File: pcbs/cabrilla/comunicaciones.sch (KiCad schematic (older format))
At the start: 6 parts, among them J8 UART_lora, U3 LoRa, Y2 LoRa

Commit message: Added STM32
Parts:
- added R14: 10k, Resistor_SMD:R_0805_2012Metric_Pad1.15x1.40mm_HandSolder, symbol Device:R
- added SW1: SW_Push, Button_Switch_SMD:SW_Push_1P1T_NO_6x6mm_H9.5mm, symbol Switch:SW_Push
- C6: renamed from C4; footprint Capacitor_SMD:C_0805_2012Metric -> Capacitor_SMD:C_0805_2012Metric_Pad1.15x1.40mm_HandSolder
- C7: renamed from C5; footprint Capacitor_SMD:C_0805_2012Metric -> Capacitor_SMD:C_0805_2012Metric_Pad1.15x1.40mm_HandSolder
- U3: renamed from U?; footprint (none) -> elementos:lorabee
- renumbered U3 to COM1, J8 to deb_com1
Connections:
- net +3V3: now also U3.1 (3.3v), R14.1
- net GND: now also U3.10 (GND), SW1.2
- net rx_lora: now also COM1.3 (PD1); no longer COM1.2 (PD0)
- net tx_lora: now also COM1.2 (PD0); no longer COM1.3 (PD1)
- net at COM1.1 (PC6/~RESET): now also R14.2, SW1.1
- net SS_lora: now reaches COM1.16 (PB2)
- net SS_lora: now also U3.17 (NSS)
- net MOSI: now reaches COM1.17 (PB3)
- net MOSI: now also U3.11 (MOSI)
- net MISO: now reaches COM1.18 (PB4)
- net MISO: now also U3.4 (MISO)
- net SCK: now reaches COM1.19 (PB5)
- net SCK: now also U3.18 (SCK)
- no-connect marks 0 -> 12
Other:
- note added: "rx, tx con respecto al STM32\n"
- moved on the sheet: U3
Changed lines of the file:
@@
 	4800 4250 5100 4250
 Text Label 5100 4150 2    50   ~ 0
+tx_lora
+Text Label 5100 4250 2    50   ~ 0
 rx_lora
-Text Label 5100 4250 2    50   ~ 0
-tx_lora
 Connection ~ 4250 5300
 Wire Wire Line
@@
 P 4250 5300
 AR Path="/5D8B0DC7" Ref="#PWR?"  Part="1"
-AR Path="/5D8ABBE4/5D8B0DC7" Ref="#PWR015"  Part="1"
-F 0 "#PWR015" H 4250 5050 50  0001 C CNN
+AR Path="/5D8ABBE4/5D8B0DC7" Ref="#PWR025"  Part="1"
+F 0 "#PWR025" H 4250 5050 50  0001 C CNN
 F 1 "GND" H 4255 5127 50  0000 C CNN
 F 2 "" H 4250 5300 50  0001 C CNN
@@
 $EndComp
 $Comp
-L MCU_Microchip_ATmega:ATmega8A-PU U?
+L MCU_Microchip_ATmega:ATmega8A-PU COM?
 U 1 1 5D8B0DCF
 P 4200 3850
-AR Path="/5D8B0DCF" Ref="U?"  Part="1"
-AR Path="/5D8ABBE4/5D8B0DCF" Ref="U3"  Part="1"
-F 0 "U3" H 4200 5431 50  0000 C CNN
+AR Path="/5D8B0DCF" Ref="COM?"  Part="1"
+AR Path="/5D8ABBE4/5D8B0DCF" Ref="COM1"  Part="1"
+F 0 "COM1" H 4200 5431 50  0000 C CNN
 F 1 "LoRa" H 4200 5340 50  0000 C CNN
 F 2 "Package_DIP:DIP-28_W7.62mm_Socket" H 4200 3850 50  0001 C CIN
@@
 P 1450 6400
 AR Path="/5D989311/5D8B0DDD" Ref="C?"  Part="1"
-AR Path="/5D8ABBE4/5D8B0DDD" Ref="C5"  Part="1"
-F 0 "C5" V 1290 6400 50  0000 C CNN
+AR Path="/5D8ABBE4/5D8B0DDD" Ref="C7"  Part="1"
+F 0 "C7" V 1290 6400 50  0000 C CNN
 F 1 "22pF" V 1199 6400 50  0000 C CNN
-F 2 "Capacitor_SMD:C_0805_2012Metric" H 1488 6250 50  0001 C CNN
+F 2 "Capacitor_SMD:C_0805_2012Metric_Pad1.15x1.40mm_HandSolder" H 1488 6250 50  0001 C CNN
 F 3 "~" H 1450 6400 50  0001 C CNN
 	1    1450 6400
@@
 P 1150 6400
 AR Path="/5D989311/5D8B0DE3" Ref="C?"  Part="1"
-AR Path="/5D8ABBE4/5D8B0DE3" Ref="C4"  Part="1"
-F 0 "C4" V 1402 6400 50  0000 C CNN
+AR Path="/5D8ABBE4/5D8B0DE3" Ref="C6"  Part="1"
+F 0 "C6" V 1402 6400 50  0000 C CNN
 F 1 "22pF" V 1311 6400 50  0000 C CNN
-F 2 "Capacitor_SMD:C_0805_2012Metric" V 1310 6400 50  0001 C CNN
+F 2 "Capacitor_SMD:C_0805_2012Metric_Pad1.15x1.40mm_HandSolder" V 1310 6400 50  0001 C CNN
 F 3 "~" H 1150 6400 50  0001 C CNN
 	1    1150 6400
@@
 P 1300 6650
 AR Path="/5D989311/5D8B0DF1" Ref="#PWR?"  Part="1"
-AR Path="/5D8ABBE4/5D8B0DF1" Ref="#PWR013"  Part="1"
-F 0 "#PWR013" H 1300 6400 50  0001 C CNN
+AR Path="/5D8ABBE4/5D8B0DF1" Ref="#PWR027"  Part="1"
+F 0 "#PWR027" H 1300 6400 50  0001 C CNN
 F 1 "GND" H 1305 6477 50  0000 C CNN
 F 2 "" H 1300 6650 50  0001 C CNN
@@
 $EndComp
 Text HLabel 5100 4150 2    50   Input ~ 0
+tx_lora
+Text HLabel 5100 4250 2    50   Input ~ 0
 rx_lora
-Text HLabel 5100 4250 2    50   Input ~ 0
-tx_lora
 Text Label 1450 5900 1    50   ~ 0
 osc_2
@@
 osc_1
 $Comp
-L Connector:Conn_01x03_Male J?
+L Connector:Conn_01x03_Male deb_com?
 U 1 1 5D8B0AA2
 P 2750 6200
-AR Path="/5D8B0AA2" Ref="J?"  Part="1"
-AR Path="/5D8ABBE4/5D8B0AA2" Ref="J8"  Part="1"
-F 0 "J8" V 2812 6013 50  0000 R CNN
+AR Path="/5D8B0AA2" Ref="deb_com?"  Part="1"
+AR Path="/5D8ABBE4/5D8B0AA2" Ref="deb_com1"  Part="1"
+F 0 "deb_com1" V 2812 6013 50  0000 R CNN
 F 1 "UART_lora" V 2903 6013 50  0000 R CNN
 F 2 "Connector_PinHeader_2.54mm:PinHeader_1x03_P2.54mm_Vertical" H 2750 6200 50  0001 C CNN
@@
 P 2850 6500
 AR Path="/5D8B0AAB" Ref="#PWR?"  Part="1"
-AR Path="/5D8ABBE4/5D8B0AAB" Ref="#PWR014"  Part="1"
-F 0 "#PWR014" H 2850 6250 50  0001 C CNN
+AR Path="/5D8ABBE4/5D8B0AAB" Ref="#PWR026"  Part="1"
+F 0 "#PWR026" H 2850 6250 50  0001 C CNN
 F 1 "GND" H 2855 6327 50  0000 C CNN
 F 2 "" H 2850 6500 50  0001 C CNN
@@
 $EndComp
 $Comp
-L power:+3.3V #PWR0102
+L power:+3.3V #PWR022
 U 1 1 5D8AD624
 P 4250 2150
-F 0 "#PWR0102" H 4250 2000 50  0001 C CNN
+F 0 "#PWR022" H 4250 2000 50  0001 C CNN
 F 1 "+3.3V" H 4265 2323 50  0000 C CNN
 F 2 "" H 4250 2150 50  0001 C CNN
@@
 $EndComp
 $Comp
-L elementos:lorabee U?
+L elementos:lorabee U3
 U 1 1 5D8B69A5
-P 8150 2150
-F 0 "U?" H 8150 2415 50  0000 C CNN
-F 1 "lorabee" H 8150 2324 50  0000 C CNN
-F 2 "" H 8150 1050 50  0001 C CNN
-F 3 "" H 8150 1050 50  0001 C CNN
-	1    8150 2150
-	1    0    0    -1
-$EndComp
+P 8650 2700
+F 0 "U3" H 8650 2965 50  0000 C CNN
+F 1 "lorabee" H 8650 2874 50  0000 C CNN
+F 2 "elementos:lorabee" H 8650 1600 50  0001 C CNN
+F 3 "" H 8650 1600 50  0001 C CNN
+	1    8650 2700
+	1    0    0    -1
+$EndComp
+Text Notes 5100 4100 0    50   ~ 0
+rx, tx con respecto al STM32\n
+Wire Wire Line
+	4800 2950 5150 2950
+Wire Wire Line
+	4800 3050 5150 3050
+Wire Wire Line
+	4800 3150 5150 3150
+Wire Wire Line
+	4800 3250 5150 3250
+Text Label 5150 2950 2    50   ~ 0
+SS_lora
+Text Label 5150 3050 2    50   ~ 0
+MOSI
+Text Label 5150 3150 2    50   ~ 0
+MISO
+Text Label 5150 3250 2    50   ~ 0
+SCK
+Wire Wire Line
+	9050 3000 9350 3000
+Wire Wire Line
+	9050 3600 9250 3600
+Wire Wire Line
+	8250 3000 8050 3000
+Wire Wire Line
+	9050 2900 9200 2900
+Text Label 9350 3000 2    50   ~ 0
+SS_lora
+Text Label 9250 3600 2    50   ~ 0
+MOSI
+Text Label 8050 3000 0    50   ~ 0
+MISO
+Text Label 9200 2900 2    50   ~ 0
+SCK
+$Comp
+L power:+3.3V #PWR023
+U 1 1 5D8F4B83
+P 8150 2700
+F 0 "#PWR023" H 8150 2550 50  0001 C CNN
+F 1 "+3.3V" H 8165 2873 50  0000 C CNN
+F 2 "" H 8150 2700 50  0001 C CNN
+F 3 "" H 8150 2700 50  0001 C CNN
+	1    8150 2700
+	1    0    0    -1
+$EndComp
+Wire Wire Line
+	8250 2700 8150 2700
+$Comp
+L power:GND #PWR024
+U 1 1 5D8F6C16
+P 8150 3600
+F 0 "#PWR024" H 8150 3350 50  0001 C CNN
+F 1 "GND" H 8155 3427 50  0000 C CNN
+F 2 "" H 8150 3600 50  0001 C CNN
+F 3 "" H 8150 3600 50  0001 C CNN
+	1    8150 3600
+	1    0    0    -1
+$EndComp
+Wire Wire Line
+	8250 3600 8150 3600
+NoConn ~ 8250 2800
+NoConn ~ 8250 3200
+NoConn ~ 8250 3300
+NoConn ~ 8250 3400
+NoConn ~ 8250 3500
+NoConn ~ 9050 3400
+NoConn ~ 9050 3300
+NoConn ~ 9050 3200
+NoConn ~ 9050 3100
+NoConn ~ 9050 2800
+NoConn ~ 9050 2700
+NoConn ~ 8250 2900
+$Comp
+L Switch:SW_Push SW1
+U 1 1 5D92194B
+P 2250 2950
+F 0 "SW1" V 2204 3098 50  0000 L CNN
+F 1 "SW_Push" V 2295 3098 50  0000 L CNN
+F 2 "Button_Switch_SMD:SW_Push_1P1T_NO_6x6mm_H9.5mm" H 2250 3150 50  0001 C CNN
+F 3 "~" H 2250 3150 50  0001 C CNN
+	1    2250 2950
+	0    1    1    0
+$EndComp
+$Comp
+L Device:R R14
+U 1 1 5D92303F
+P 2250 2600
+F 0 "R14" H 2320 2646 50  0000 L CNN
+F 1 "10k" H 2320 2555 50  0000 L CNN
+F 2 "Resistor_SMD:R_0805_2012Metric_Pad1.15x1.40mm_HandSolder" V 2180 2600 50  0001 C CNN
+F 3 "~" H 2250 2600 50  0001 C CNN
+	1    2250 2600
+	1    0    0    -1
+$EndComp
+Connection ~ 2250 2750
+Wire Wire Line
+	2250 2750 3600 2750
+$Comp
+L power:GND #PWR0113
+U 1 1 5D924AFA
+P 2250 3150
+F 0 "#PWR0113" H 2250 2900 50  0001 C CNN
+F 1 "GND" H 2255 2977 50  0000 C CNN
+F 2 "" H 2250 3150 50  0001 C CNN
+F 3 "" H 2250 3150 50  0001 C CNN
+	1    2250 3150
+	1    0    0    -1
+$EndComp
+$Comp
+L power:+3.3V #PWR0114
+U 1 1 5D924E3E
+P 2250 2450
+F 0 "#PWR0114" H 2250 2300 50  0001 C CNN
+F 1 "+3.3V" H 2265 2623 50  0000 C CNN
+F 2 "" H 2250 2450 50  0001 C CNN
+F 3 "" H 2250 2450 50  0001 C CNN
+	1    2250 2450
+	1    0    0    -1
+$EndComp

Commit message: ixed
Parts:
- Y2: footprint Crystal:Crystal_HC49-4H_Vertical -> Crystal:Crystal_SMD_HC49-SD
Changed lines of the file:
@@
 F 0 "Y2" H 1300 6318 50  0000 C CNN
 F 1 "LoRa" H 1300 6227 50  0000 C CNN
-F 2 "Crystal:Crystal_HC49-4H_Vertical" H 1300 6050 50  0001 C CNN
+F 2 "Crystal:Crystal_SMD_HC49-SD" H 1300 6050 50  0001 C CNN
 F 3 "~" H 1300 6050 50  0001 C CNN
 	1    1300 6050

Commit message: 80
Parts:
- Y2: footprint Crystal:Crystal_SMD_HC49-SD -> Crystal:Crystal_SMD_HC49-SD_HandSoldering
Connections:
- net rx_lora: now also COM1.2 (PD0); no longer COM1.3 (PD1)
- net tx_lora: now also COM1.3 (PD1); no longer COM1.2 (PD0)
- no-connect marks 12 -> 27
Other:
- note removed: "rx, tx con respecto al STM32\n"
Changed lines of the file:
@@
 	4800 4250 5100 4250
 Text Label 5100 4150 2    50   ~ 0
+rx_lora
+Text Label 5100 4250 2    50   ~ 0
 tx_lora
-Text Label 5100 4250 2    50   ~ 0
-rx_lora
 Connection ~ 4250 5300
 Wire Wire Line
@@
 F 0 "Y2" H 1300 6318 50  0000 C CNN
 F 1 "LoRa" H 1300 6227 50  0000 C CNN
-F 2 "Crystal:Crystal_SMD_HC49-SD" H 1300 6050 50  0001 C CNN
+F 2 "Crystal:Crystal_SMD_HC49-SD_HandSoldering" H 1300 6050 50  0001 C CNN
 F 3 "~" H 1300 6050 50  0001 C CNN
 	1    1300 6050
@@
 $EndComp
 Text HLabel 5100 4150 2    50   Input ~ 0
+rx_lora
+Text HLabel 5100 4250 2    50   Input ~ 0
 tx_lora
-Text HLabel 5100 4250 2    50   Input ~ 0
-rx_lora
 Text Label 1450 5900 1    50   ~ 0
 osc_2
@@
 	1    0    0    -1
 $EndComp
-Text Notes 5100 4100 0    50   ~ 0
-rx, tx con respecto al STM32\n
 Wire Wire Line
 	4800 2950 5150 2950
@@
 	1    0    0    -1
 $EndComp
+NoConn ~ 4800 2750
+NoConn ~ 4800 2850
+NoConn ~ 3600 3350
+NoConn ~ 4800 3450
+NoConn ~ 4800 3550
+NoConn ~ 4800 3650
+NoConn ~ 4800 3750
+NoConn ~ 4800 3850
+NoConn ~ 4800 3950
+NoConn ~ 4800 4350
+NoConn ~ 4800 4450
+NoConn ~ 4800 4550
+NoConn ~ 4800 4650
+NoConn ~ 4800 4750
+NoConn ~ 4800 4850
 $EndSCHEMATC

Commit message: Updated footprints
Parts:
- U3: symbol elementos:lorabee -> cabrilla-rescue:lorabee-elementos
- Y2: footprint Crystal:Crystal_SMD_HC49-SD_HandSoldering -> Crystal:Crystal_HC49-4H_Vertical
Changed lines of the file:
@@
 EESchema Schematic File Version 4
 LIBS:cabrilla-cache
-EELAYER 30 0
+EELAYER 29 0
 EELAYER END
 $Descr A4 11693 8268
@@
 F 0 "Y2" H 1300 6318 50  0000 C CNN
 F 1 "LoRa" H 1300 6227 50  0000 C CNN
-F 2 "Crystal:Crystal_SMD_HC49-SD_HandSoldering" H 1300 6050 50  0001 C CNN
+F 2 "Crystal:Crystal_HC49-4H_Vertical" H 1300 6050 50  0001 C CNN
 F 3 "~" H 1300 6050 50  0001 C CNN
 	1    1300 6050
@@
 $EndComp
 $Comp
-L elementos:lorabee U3
+L cabrilla-rescue:lorabee-elementos U3
 U 1 1 5D8B69A5
 P 8650 2700

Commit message: Routed
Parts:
- SW1: footprint Button_Switch_SMD:SW_Push_1P1T_NO_6x6mm_H9.5mm -> Button_Switch_SMD:SW_Push_1P1T_NO_CK_KSC6xxJ
- U3: symbol cabrilla-rescue:lorabee-elementos -> cabrilla-rescue:lorabee-elementos-cabrilla-rescue
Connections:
- net RESET: now reaches COM1.11 (PD5)
- net RESET: now also U3.5 (RESET)
- net DIO0: now reaches COM1.4 (PD2)
- net DIO0: now also U3.12 (DIO0)
- no-connect marks 27 -> 25
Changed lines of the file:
@@
 EESchema Schematic File Version 4
 LIBS:cabrilla-cache
-EELAYER 29 0
+EELAYER 30 0
 EELAYER END
 $Descr A4 11693 8268
@@
 $EndComp
 $Comp
-L cabrilla-rescue:lorabee-elementos U3
+L cabrilla-rescue:lorabee-elementos-cabrilla-rescue U3
 U 1 1 5D8B69A5
 P 8650 2700
@@
 F 0 "SW1" V 2204 3098 50  0000 L CNN
 F 1 "SW_Push" V 2295 3098 50  0000 L CNN
-F 2 "Button_Switch_SMD:SW_Push_1P1T_NO_6x6mm_H9.5mm" H 2250 3150 50  0001 C CNN
+F 2 "Button_Switch_SMD:SW_Push_1P1T_NO_CK_KSC6xxJ" H 2250 3150 50  0001 C CNN
 F 3 "~" H 2250 3150 50  0001 C CNN
 	1    2250 2950
@@
 NoConn ~ 4800 3850
 NoConn ~ 4800 3950
-NoConn ~ 4800 4350
 NoConn ~ 4800 4450
 NoConn ~ 4800 4550
-NoConn ~ 4800 4650
 NoConn ~ 4800 4750
 NoConn ~ 4800 4850
+Text Label 4950 4350 0    50   ~ 0
+DIO0
+Wire Wire Line
+	4950 4350 4800 4350
+Wire Wire Line
+	9050 3500 9250 3500
+Text Label 9250 3500 2    50   ~ 0
+DIO0
+Text Label 5050 4650 2    50   ~ 0
+RESET
+Wire Wire Line
+	5050 4650 4800 4650
+Text Label 8000 3100 0    50   ~ 0
+RESET
+Wire Wire Line
+	8250 3100 8000 3100
 $EndSCHEMATC

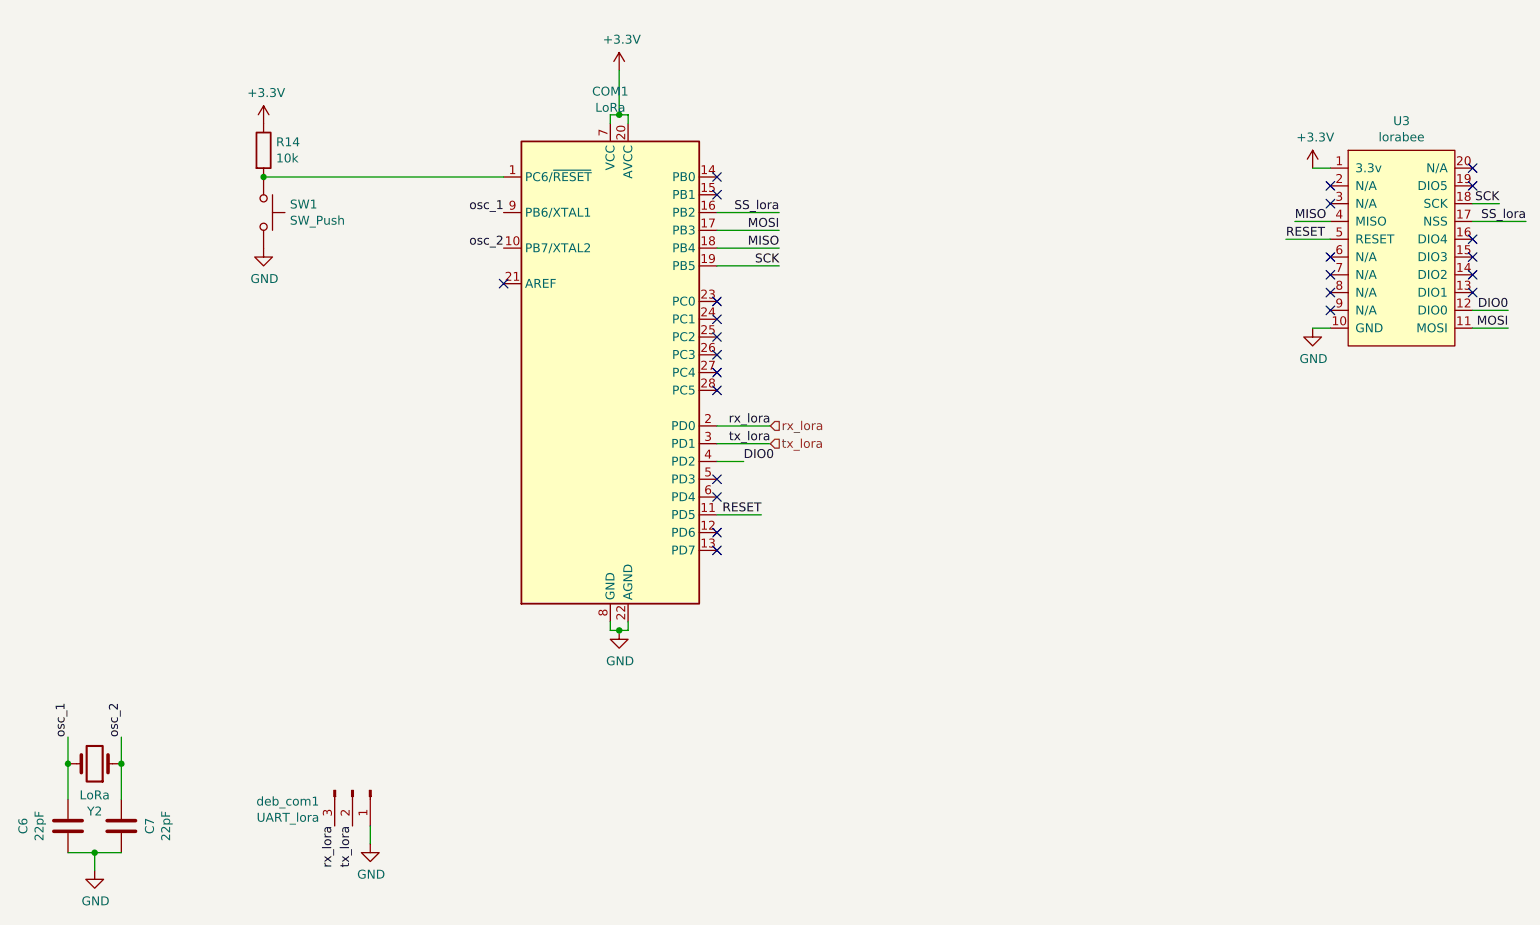
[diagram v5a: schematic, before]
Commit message: Cambiados los parámetros de rutero
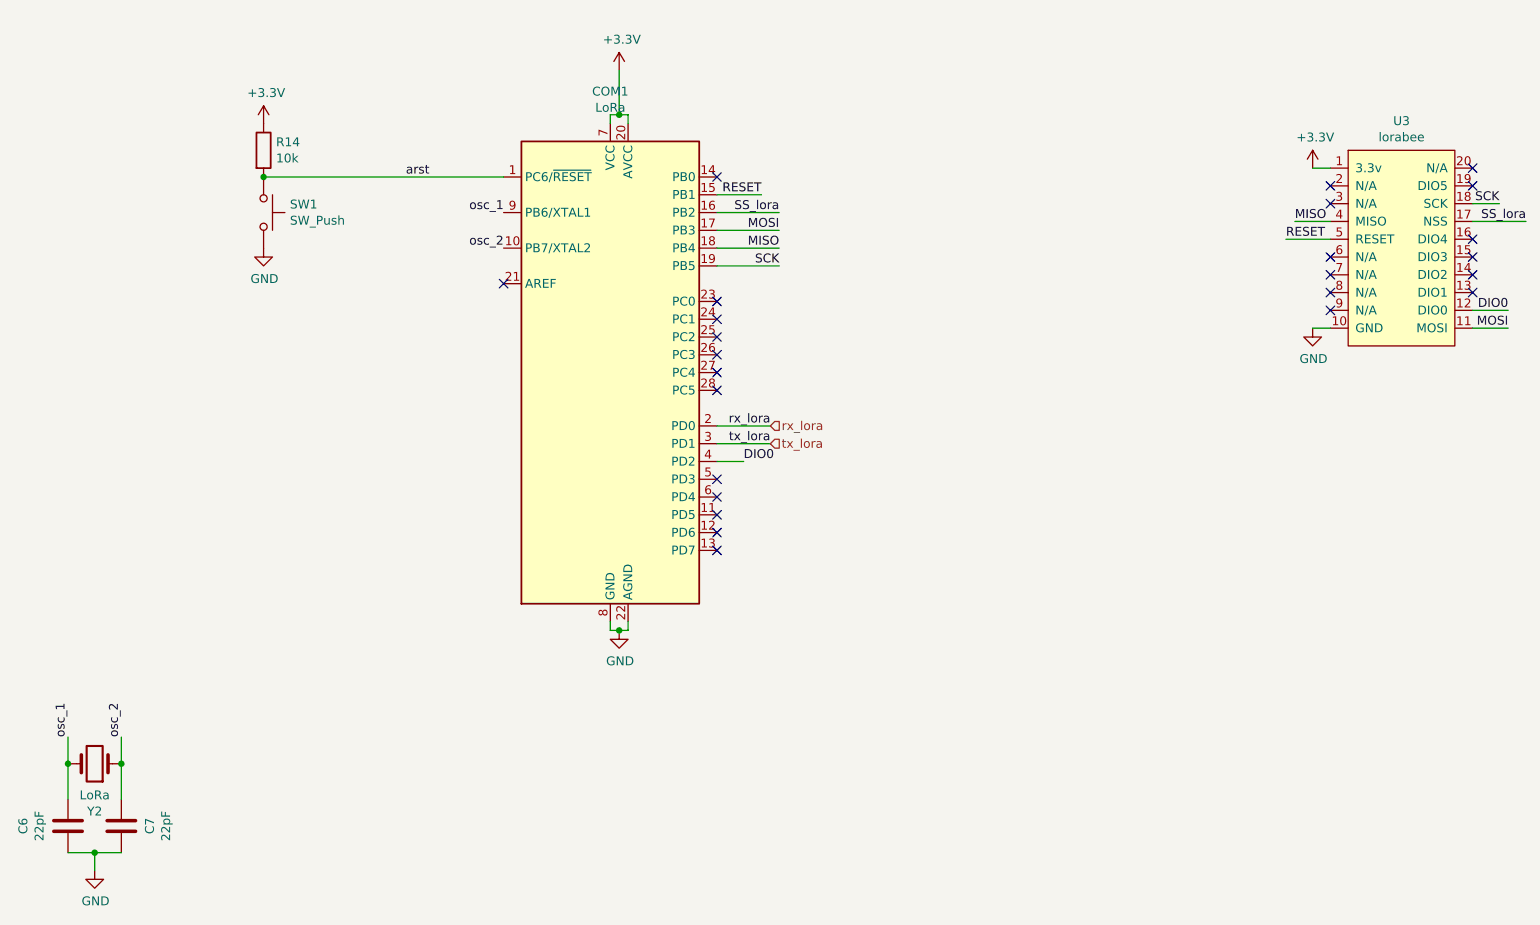
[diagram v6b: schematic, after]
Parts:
- removed deb_com1: UART_lora, Connector_PinHeader_2.54mm:PinHeader_1x03_P2.54mm_Vertical, symbol Connector:Conn_01x03_Male
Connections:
- net RESET: now also COM1.15 (PB1); no longer COM1.11 (PD5)
- net arst: now reaches COM1.1 (PC6/~RESET), R14.2, SW1.1
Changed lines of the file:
@@
 osc_1
-$Comp
-L Connector:Conn_01x03_Male deb_com?
-U 1 1 5D8B0AA2
-P 2750 6200
-AR Path="/5D8B0AA2" Ref="deb_com?"  Part="1"
-AR Path="/5D8ABBE4/5D8B0AA2" Ref="deb_com1"  Part="1"
-F 0 "deb_com1" V 2812 6013 50  0000 R CNN
-F 1 "UART_lora" V 2903 6013 50  0000 R CNN
-F 2 "Connector_PinHeader_2.54mm:PinHeader_1x03_P2.54mm_Vertical" H 2750 6200 50  0001 C CNN
-F 3 "~" H 2750 6200 50  0001 C CNN
-	1    2750 6200
-	0    1    1    0
-$EndComp
-Text Label 2650 6400 3    50   ~ 0
-rx_lora
-Text Label 2750 6400 3    50   ~ 0
-tx_lora
-Wire Wire Line
-	2850 6400 2850 6500
-$Comp
-L power:GND #PWR?
-U 1 1 5D8B0AAB
-P 2850 6500
-AR Path="/5D8B0AAB" Ref="#PWR?"  Part="1"
-AR Path="/5D8ABBE4/5D8B0AAB" Ref="#PWR026"  Part="1"
-F 0 "#PWR026" H 2850 6250 50  0001 C CNN
-F 1 "GND" H 2855 6327 50  0000 C CNN
-F 2 "" H 2850 6500 50  0001 C CNN
-F 3 "" H 2850 6500 50  0001 C CNN
-	1    2850 6500
-	1    0    0    -1
-$EndComp
 $Comp
 L power:+3.3V #PWR022
@@
 $EndComp
 NoConn ~ 4800 2750
-NoConn ~ 4800 2850
 NoConn ~ 3600 3350
 NoConn ~ 4800 3450
@@
 Text Label 9250 3500 2    50   ~ 0
 DIO0
-Text Label 5050 4650 2    50   ~ 0
+Text Label 5050 2850 2    50   ~ 0
 RESET
 Wire Wire Line
-	5050 4650 4800 4650
+	5050 2850 4800 2850
 Text Label 8000 3100 0    50   ~ 0
 RESET
 Wire Wire Line
 	8250 3100 8000 3100
+NoConn ~ 4800 4650
+Text Label 3050 2750 0    50   ~ 0
+arst
 $EndSCHEMATC
